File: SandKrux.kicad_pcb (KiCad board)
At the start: 2 copper layers, 58.3 x 98.2 mm, 175 parts, among them CN2 1.25mm-2P socket, IC1 TROPIC01_chip, Q1 S8050, SW1 TL3330AF130QG, SW2 TL3330AF130QG, SW3 TL3330AF130QG, SW4 TL3330AF130QG, SW5 TL3330AF130QG, U1 K210_C913414, U10 AXP173_C3345106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

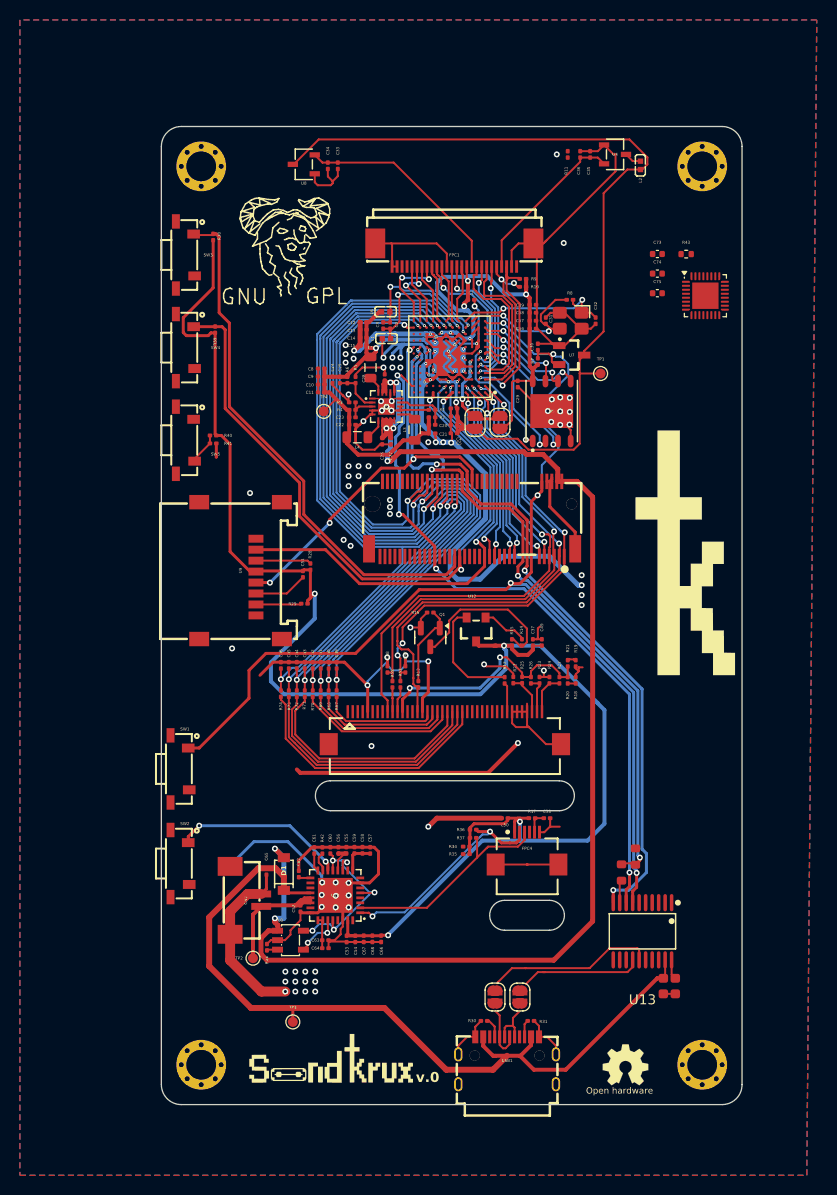
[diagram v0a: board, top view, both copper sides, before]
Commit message: ajuste de esquematico e posicionamento de componentes
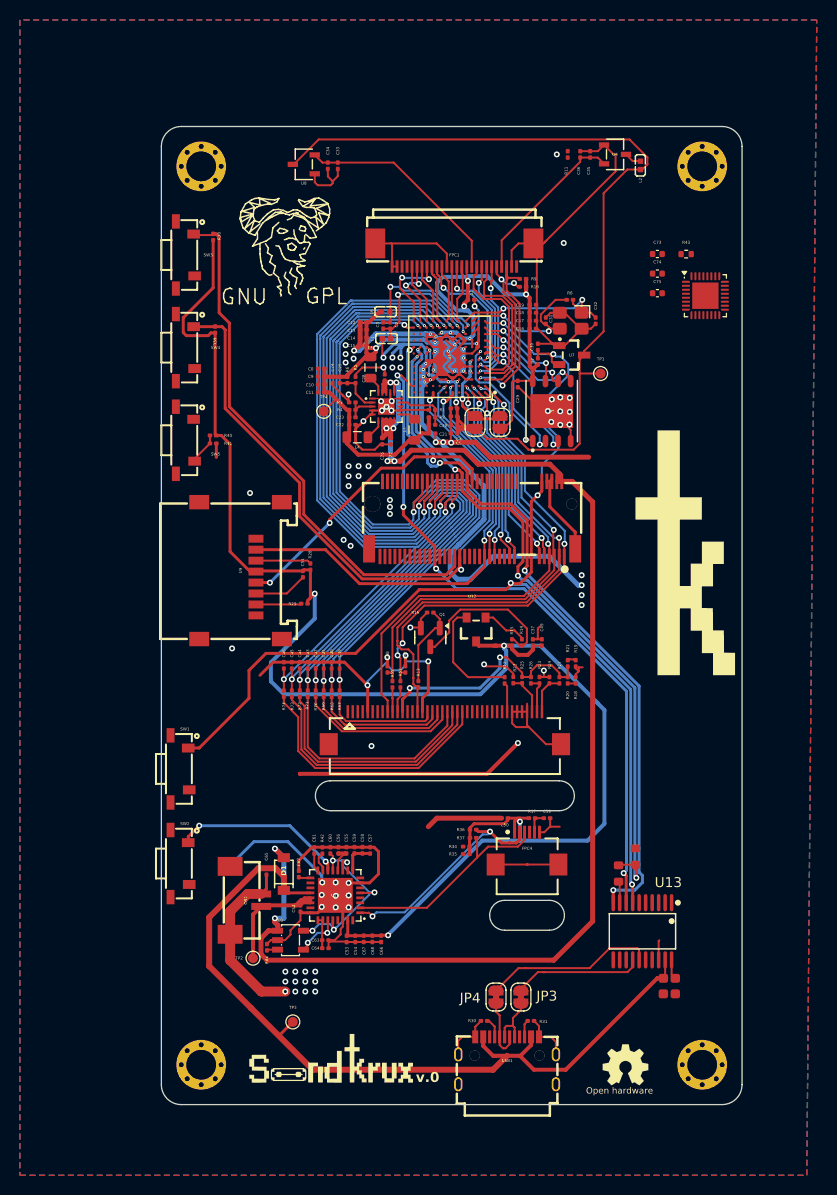
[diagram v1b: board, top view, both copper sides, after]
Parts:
- removed the JP2 at (116.2, 176.1)
- removed the JP2 at (113.7, 176.1)
- added JP3: SolderJumper_2_Bridged, Jumper:SolderJumper-2_P1.3mm_Bridged_RoundedPad1.0x1.5mm, F.Cu at (116.3, 176.1)
- added JP4: SolderJumper_2_Bridged, Jumper:SolderJumper-2_P1.3mm_Bridged_RoundedPad1.0x1.5mm, F.Cu at (113.8, 176.1)
- moved R32 0.32 mm to (126.1, 163.7)
- moved C43 0.30 mm to (94.9, 142.8)
- moved R71 0.30 mm to (94.9, 145.6)
- moved C39 0.30 mm to (98.1, 142.8)
- moved C40 0.30 mm to (97.3, 142.8)
- moved C41 0.30 mm to (96.5, 142.8)
- moved C42 0.30 mm to (95.7, 142.8)
- moved C44 0.30 mm to (94.1, 142.8)
- moved C45 0.30 mm to (93.3, 142.8)
- moved C46 0.30 mm to (92.5, 142.8)
- moved R67 0.30 mm to (98.1, 145.6)
- moved R68 0.30 mm to (97.3, 145.7)
- moved R69 0.30 mm to (96.5, 145.7)
- moved R70 0.30 mm to (95.7, 145.7)
- moved R72 0.30 mm to (94.1, 145.6)
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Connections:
- U13 pad 14: /USBDP -> Net-(JP3-B)
- U13 pad 15: /USBDM -> Net-(JP4-B)
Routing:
- net GND: track 488.4 -> 506.2 mm
- net Net-(JP4-B): track 0.00 -> 17.3 mm
- net /USBDM: track 22.6 -> 6.36 mm
- net Net-(JP3-B): track 0.00 -> 13.2 mm
- net /USBDP: track 17.1 -> 5.57 mm
- net /5V: track 139.3 -> 141.0 mm, vias 7 -> 8
- net /SPI1_MISO: track 39.9 -> 41.2 mm
- net /CH552_RX0: track 73.7 -> 72.5 mm
- net /LCD_D1: track 74.1 -> 73.1 mm
- net /ISP_RX: track 69.4 -> 68.4 mm
- net /LCD_WR: track 47.6 -> 46.7 mm
- net /BOOT: track 69.7 -> 68.8 mm
- net /LCD_D3: track 77.1 -> 76.2 mm
- net Net-(FPC3-Pad21): track 22.8 -> 21.9 mm
- net /SPI1_CS_TF: track 47.0 -> 46.2 mm
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
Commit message: CNC AND PRINTER
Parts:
- added CN3: 1.25mm-2P socket, easyeda2kicad:CONN-SMD_1.25T-2P, F.Cu at (88.7, 166.4)
- CN2: value 1.25mm-2P socket -> SM02B-PASS-TBT(LF)(SN); footprint easyeda2kicad:CONN-SMD_1.25T-2P -> easyeda2kicad:CONN-SMD_SM02B-PASS-TBT
- moved CN2 70.3 mm to (93.2, 96.2), turned to 180 degrees
- moved U8 31.3 mm to (125.6, 96.1), turned to 180 degrees
- moved C34 26.5 mm to (123.2, 96.0), turned to -90 degrees
- moved C33 24.5 mm to (122.2, 96.0), turned to -90 degrees
- moved REF** 18.8 mm to (90.3, 118.2)
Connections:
- CN2 pad 1: /VBAT -> /PRINTER
- U1 pad G12: /k210/IO_7 -> /PRINTER
- U12 pad 71: unconnected-(U12-Pad71) -> /PRINTER
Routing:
- net /PRINTER: track 0.00 -> 59.4 mm, vias 0 -> 2
- net +3.3V: track 103.3 -> 64.6 mm
- net GND: track 506.2 -> 496.2 mm, vias 88 -> 87
- net /k210/CMOS-AVDD: track 16.9 -> 23.4 mm
- net /k210/CMOS-DVDD: track 21.9 -> 17.7 mm
- net Net-(U1-VSSPLL): track 15.6 -> 16.7 mm
- net Net-(U1-VDDPLL): track 14.1 -> 14.7 mm
